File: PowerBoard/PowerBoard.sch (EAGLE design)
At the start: 88 parts, among them IC1 MCP16311, IC2 MCP16311, IC3 DS2431P, U1 BQ24090, U2 MCP1726, U3 ATTINY85V, X2 MICROMATCH-4, X3 MICROMATCH-4

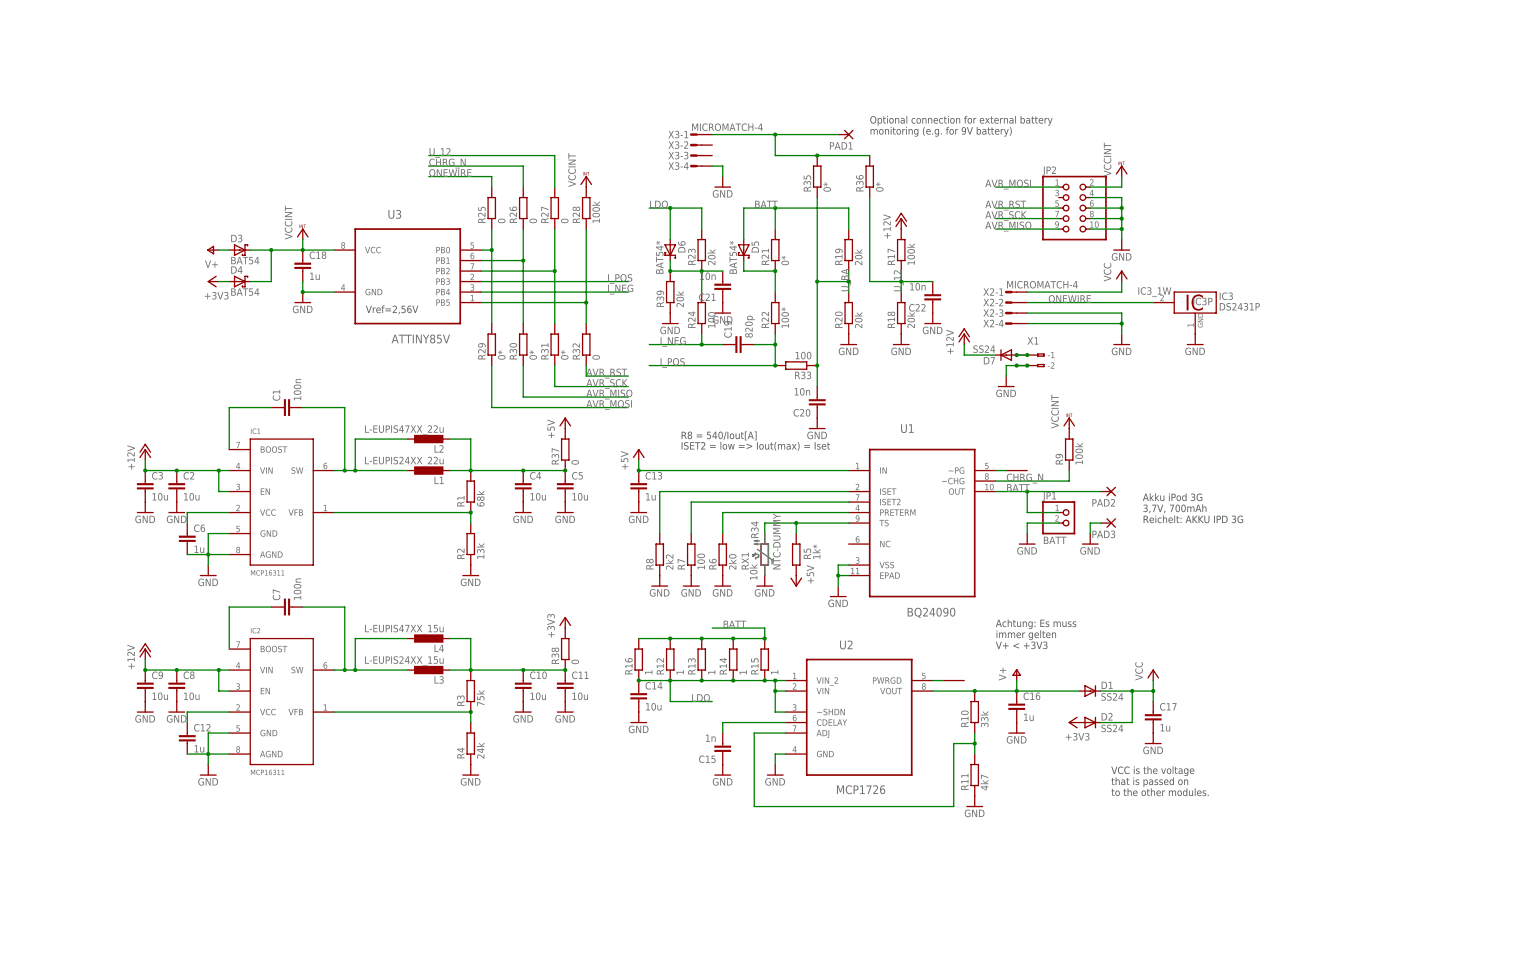
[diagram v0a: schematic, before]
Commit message: Added inputs for Rev2 of PowerBoard to schematic
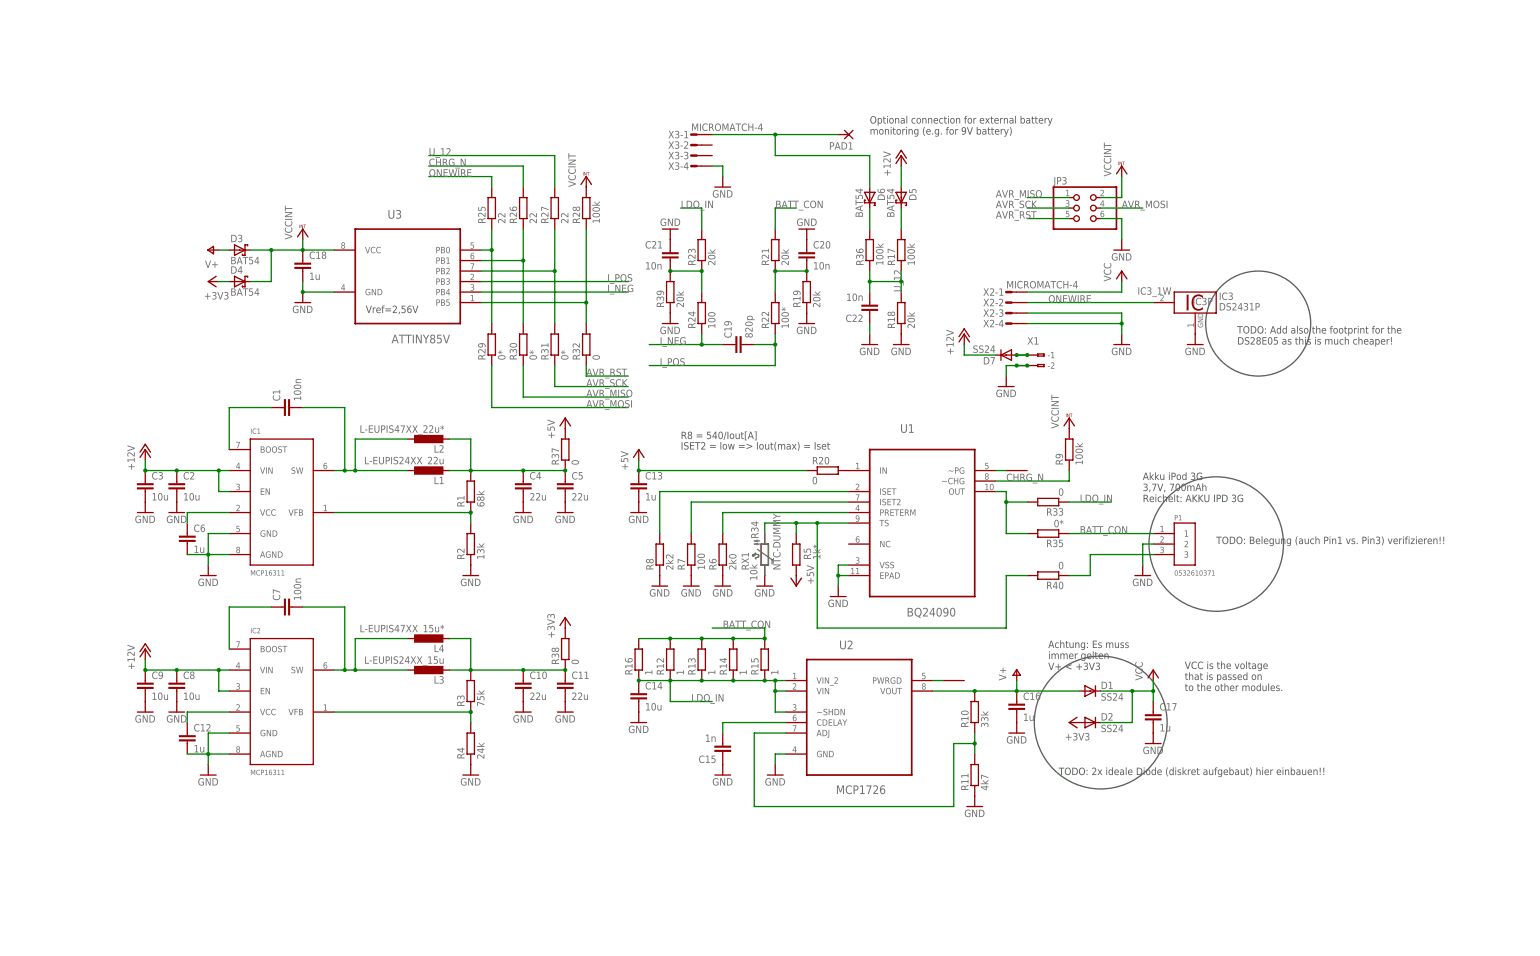
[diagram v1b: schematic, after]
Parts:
- removed JP1: BATT, pinhead:PINHD-1X2
- removed JP2: (no value), pinhead:PINHD-2X5
- removed PAD2, PAD3: WIREPADSMD2,54-5,08, wirepad:WIREPADSMD2,54-5,08
- added JP3: (no value), pinhead:PINHD-2X3
- added P1: 0532610371, 0532610371:0532610371
- added R40: 0, rcl:R-EU_R0603
- C10, C11, C4, C5: value 10u -> 22u
- D5, D6: value BAT54* -> BAT54
- L2: value L-EUPIS47XX_22u -> L-EUPIS47XX_22u*
- L4: value L-EUPIS47XX_15u -> L-EUPIS47XX_15u*
- R20: value 20k -> 0
- R21: value 0* -> 20k
- R25, R26, R27: value 0 -> 22
- R33: value 100 -> 0
- R36: value 0* -> 100k
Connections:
- removed net BATT: D5.A, JP1.1, PAD2.P, R12.2, R13.2, R14.2, R15.2, R16.2, R19.2, R21.2, U1.OUT
- removed net LDO: C14.1, D6.A, R12.1, R13.1, R14.1, R15.1, R16.1, R23.2, U2.VIN, U2.VIN_2, U2.~SHDN
- removed net U_BA: C20.2, R19.1, R20.2, R33.1, R35.1
- new net BATT_CON: P1.1, R12.2, R13.2, R14.2, R15.2, R16.2, R21.2
- new net LDO_IN: C14.1, R12.1, R13.1, R14.1, R15.1, R16.1, R23.2, R33.1, U2.VIN, U2.VIN_2, U2.~SHDN
- new net N$27: C20.2, R19.2, R21.1, R22.2
- new net N$28: D5.C, R17.2
- new net N$29: R20.2, U1.IN
- new net N$30: R33.2, R35.2, U1.OUT
- new net N$31: P1.3, R40.1
- net +12V: now also D5.A; no longer R17.2
- net +5V: now also R20.1; no longer U1.IN
- net AVR_MISO: no longer JP2.9
- net AVR_MOSI: no longer JP2.1
- net AVR_RST: no longer JP2.5
- net AVR_SCK: no longer JP2.7
- net GND: now also JP3.6, P1.2, R19.1; no longer JP1.2, JP2.10, JP2.4, JP2.6, JP2.8, PAD3.P, R20.1
- net I_POS: no longer R33.2
- net N$13: now also R40.2
- net N$17: now also D6.C, R36.2; no longer D5.C, R21.1, R22.2
- net N$21: no longer D6.C
- net N$24: now also D6.A; no longer R35.2, R36.2
- net VCCINT: now also JP3.2; no longer JP2.2
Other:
- note added: "TODO: 2x ideale Diode (diskret aufgebaut) hier einbauen!!"
- note added: "TODO: Add also the footprint for the DS28E05 as this is much cheaper!"
- note added: "TODO: Belegung (auch Pin1 vs. Pin3) verifizieren!!"
- moved on the sheet: C20, C21, C22, D5, D6, R19, R20, R33, R35, R36

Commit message: Optical cleanup of the schematic, added ideal diodes and some other stuff from the TODO list
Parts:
- added IC4: DS28E05, 1wire:DS28E05
- added Q1, Q3, Q4, Q6: BC857BSMD, transistor-pnp:BC857BSMD
- added Q2, Q5: IRLML6402, IRLML6402:IRLML6402
- added R41, R43, R44, R46: 47k, rcl:R-EU_R0603
- added R42, R45: 470k, rcl:R-EU_R0603
- D1, D2: value SS24 -> SS24*
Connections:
- new net N$33: Q1.C, Q2.G, R43.2
- new net N$34: Q1.B, Q3.B, R42.2
- new net N$35: Q3.C, R41.2
- new net N$37: Q4.C, Q5.G, R44.2
- new net N$38: Q4.B, Q6.B, R45.2
- new net N$39: Q6.C, R46.2
- net +3V3: now also Q5.S, Q6.E
- net AVR_MISO: now also JP3.1
- net AVR_MOSI: now also JP3.4
- net AVR_RST: now also JP3.5
- net AVR_SCK: now also JP3.3
- net BATT_CON: now also R35.1
- net GND: now also IC4P.GND, R41.1, R42.1, R43.1, R44.1, R45.1, R46.1
- net ONEWIRE: now also IC4_1W.1W
- net V+: now also Q2.S, Q3.E
- net VCC: now also Q1.E, Q2.D, Q4.E, Q5.D
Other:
- note added: "2 ideal diodes, details see simulation folder The 2 real diodes are just a fallback in case there are big peak currents during switching"
- note added: "AVR ISP connector"
- note added: "DC Input with Reverse Current protection"
- note added: "Make sure the programmer can always access the uC."
- note added: "Make sure the uC always gets at least one voltage."
- note added: "Output connector and 1-Wire Devices"
- note added: "To enhance battery life make sure that always V+ < +3V3 !!"
- note removed: "Achtung: Es muss immer gelten V+ < +3V3"
- note removed: "TODO: 2x ideale Diode (diskret aufgebaut) hier einbauen!!"
- note removed: "TODO: Add also the footprint for the DS28E05 as this is much cheaper!"
- moved on the sheet: C1, C10, C11, C12, C13, C14, C15, C16, C17, C18, C19, C2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
